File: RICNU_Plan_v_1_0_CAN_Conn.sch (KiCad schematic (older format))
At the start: 2 parts, among them J3 DF52-4S-0.8H(21)

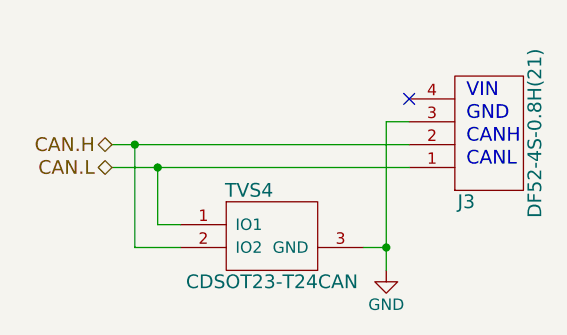
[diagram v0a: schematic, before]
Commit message: Re-routed CAN, RS-485, and debug connectors (wrong polarity in all)
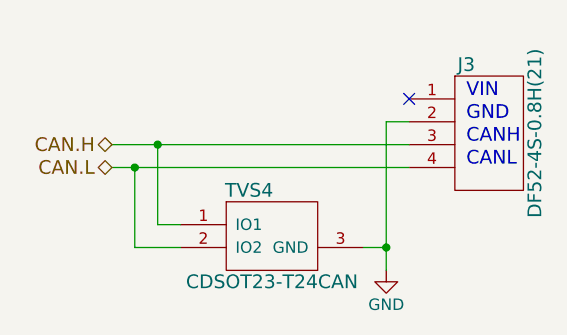
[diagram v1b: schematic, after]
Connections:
- net CAN.H: now also J3.3, TVS4.1 (IO1); no longer J3.2, TVS4.2 (IO2)
- net CAN.L: now also J3.4, TVS4.2 (IO2); no longer J3.1, TVS4.1 (IO1)
- net GND: now also J3.2; no longer J3.3
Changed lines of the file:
@@
 F 3 "" H 6700 3700 60  0001 C CNN
 	1    6700 3700
-	1    0    0    1
+	1    0    0    -1
 $EndComp
 Text Notes 6600 3550 0    60   ~ 0
@@
 	5150 4200 5350 4200
 $Comp
-L GND #PWR064
+L GND #PWR065
 U 1 1 59FAD5B0
 P 6250 4300
-F 0 "#PWR064" H 6250 4050 50  0001 C CNN
+F 0 "#PWR065" H 6250 4050 50  0001 C CNN
 F 1 "GND" H 6250 4150 50  0000 C CNN
 F 2 "" H 6250 4300 50  0001 C CNN
@@
 	6250 4200 6150 4200
 Connection ~ 6250 4200
-Connection ~ 5150 3750
-Connection ~ 5250 3850
+Connection ~ 5250 3750
+Connection ~ 5150 3850
 Wire Wire Line
-	5150 3750 5150 4200
+	5250 3750 5250 4100
 Wire Wire Line
-	5250 3850 5250 4100
+	5150 3850 5150 4200
 $EndSCHEMATC
